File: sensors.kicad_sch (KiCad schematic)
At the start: 3 parts, among them J1 Conn_Coaxial, U2 MAX-M8C

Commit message: Power Supply Speccing, IMU, Eyeballs
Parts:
- added C23: 4.7u, Capacitor_SMD:C_0805_2012Metric, symbol Device:C
- added U8: LSM6DSO32, Package_LGA:LGA-14_3x2.5mm_P0.5mm_LayoutBorder3x4y, symbol 0_airbrake_symbols:LSM6DSO32
- C7: value C -> 4.7u
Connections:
- net 3V3_MCU: now also U8.5 (VCCIO)
- net 3V3_Sensors: now also C23.1, U8.8 (VDD)
- net ACCEL_CS: now also U8.12 (CS)
- net ACCEL_SCLK: now also U8.13 (SCLK)
- net ACCEL_SDI: now also U8.14 (SDI)
- net ACCEL_SDO: now also U8.1 (SDO)
- net GND: now also C23.2, U8.2 (SDx), U8.3 (SCx), U8.6 (GND), U8.7 (GND)
- no-connect marks 6 -> 8
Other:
- moved on the sheet: J1, U2

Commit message: Release Candidate 1
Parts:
- added C25: 4.7u, Capacitor_SMD:C_0805_2012Metric, symbol Device:C
- added J4: Conn_01x03_Socket, Connector_Molex:Molex_Micro-Fit_3.0_43650-0315_1x03_P3.00mm_Vertical, symbol Connector:Conn_01x03_Socket
- added U9: BME680, Package_LGA:Bosch_LGA-8_3x3mm_P0.8mm_ClockwisePinNumbering, symbol Sensor:BME680
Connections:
- net 3V3_MCU: now also U9.2 (CSB), U9.6 (VDDIO)
- net 3V3_Sensors: now also C25.1, U9.8 (VDD)
- net GND: now also C25.2, U9.1 (GND), U9.5 (SDO), U9.7 (GND)
- net GPS_TP: now reaches U2.4 (TIMEPULSE)
- new net BME680_I2C3_SCL: U9.4 (SCK)
- new net BME680_I2C3_SDA: U9.3 (SDI)
- new net SERVO+: J4.1 (Pin_1)
- new net SERVO_POW: J4.2 (Pin_2)
- new net SERVO_SIG: J4.3 (Pin_3)
- no-connect marks 8 -> 7
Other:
- note added: "Gas/Humidity/Pressure/Temp"
- note added: "I2C Selected"
- note added: "LSB=0 Selected"
- note added: "Servo Header"
- note removed: "CHECK: NEED TIMEPULSE?"
- moved on the sheet: C23, C7, J1, U2, U8

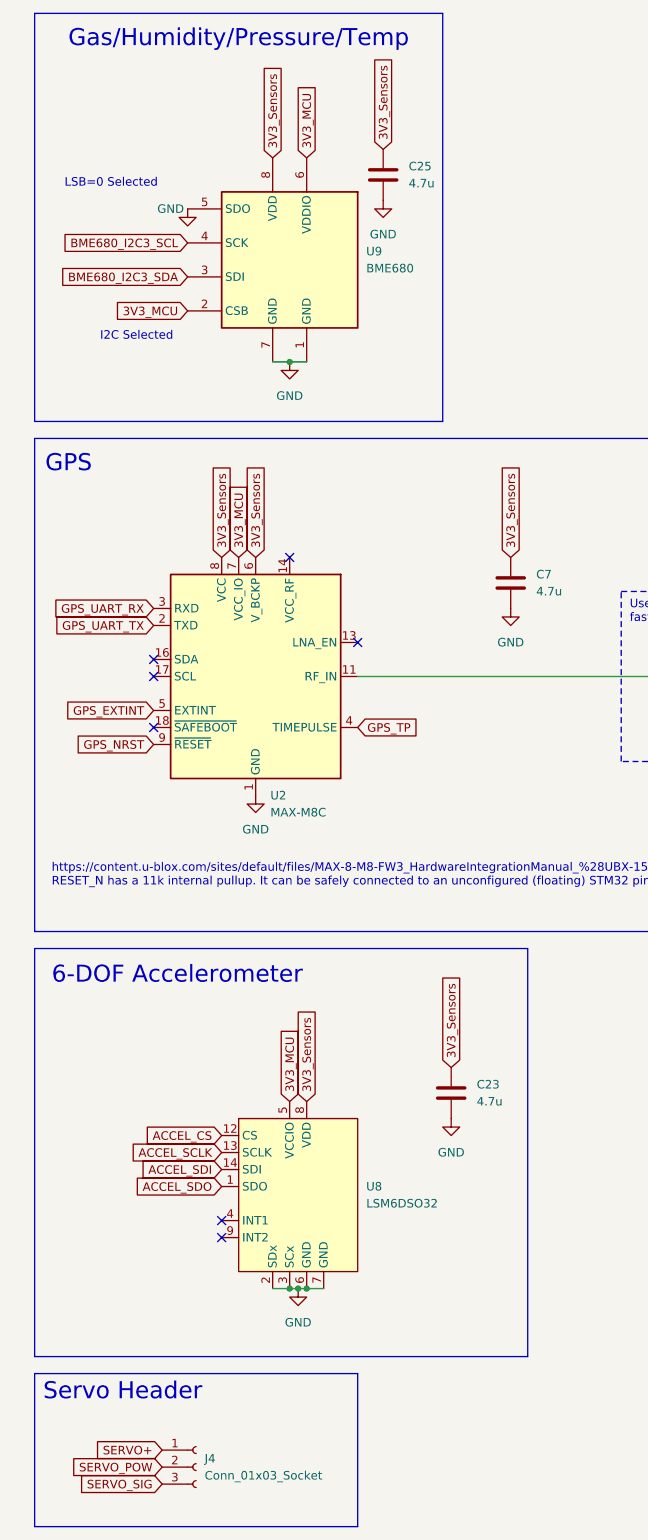
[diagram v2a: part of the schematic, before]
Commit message: Release Candidate 2
Incorporates fixes for all identified issues in the PCBR
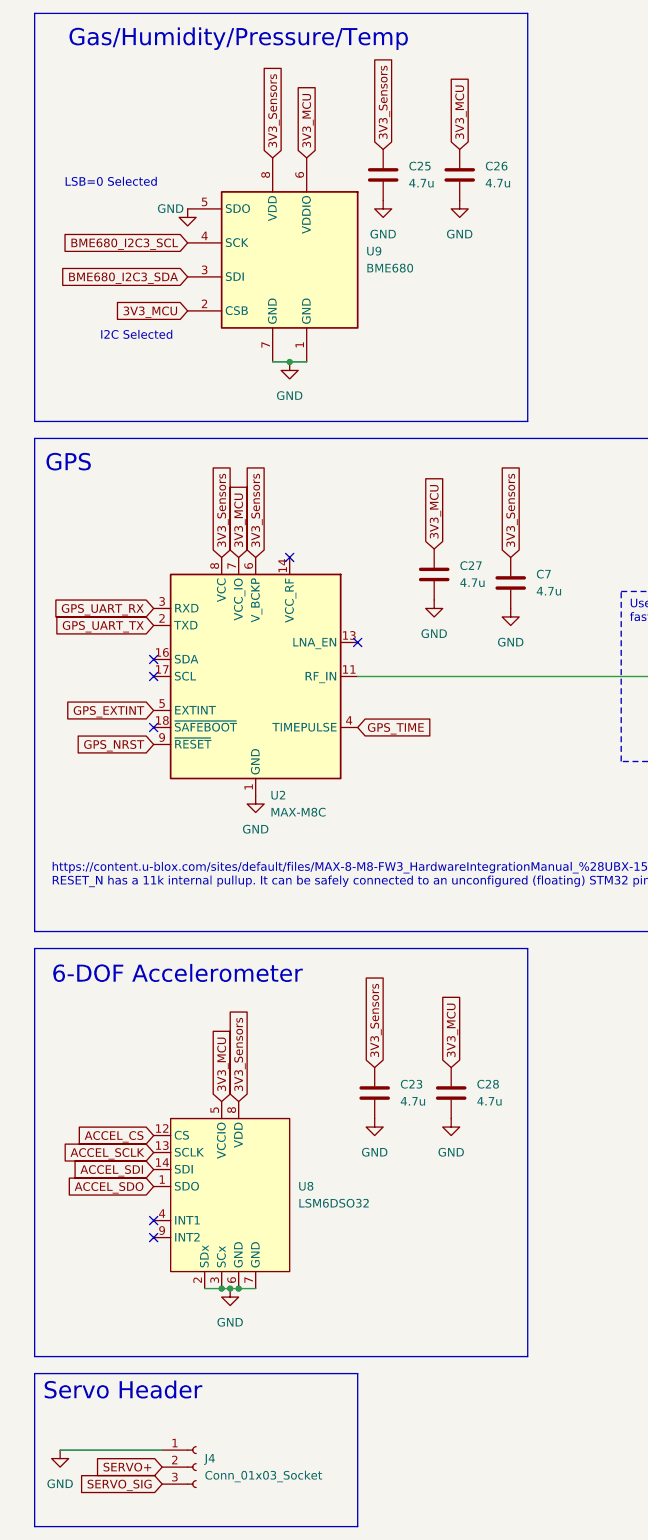
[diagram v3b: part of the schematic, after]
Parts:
- added C26, C27, C28: 4.7u, Capacitor_SMD:C_0805_2012Metric, symbol Device:C
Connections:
- net SERVO_POW is gone; now on net SERVO+: J4.2 (Pin_2)
- net 3V3_MCU: now also C26.1, C27.1, C28.1
- net GND: now also J4.1 (Pin_1), C26.2, C27.2, C28.2
- net SERVO+: no longer J4.1 (Pin_1)
- net GPS_TP renamed GPS_TIME
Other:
- moved on the sheet: C23, U8

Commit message: Release Candidate 3
Fixed name, one location with vias. Added production files in prep for merge request.
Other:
- title: Airbrakes PCB - Earendel -> Airbrakes PCB - Veðrfölnir 
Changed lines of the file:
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@@
 	(paper "B")
 	(title_block
-		(title "Airbrakes PCB - Earendel")
+		(title "Airbrakes PCB - Veðrfölnir ")
 		(date "2025-02-18")
 		(rev "v2025.01A")
